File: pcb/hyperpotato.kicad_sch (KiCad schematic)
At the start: 61 parts, among them J1 Conn_01x02_Socket, J2 Conn_01x02_Socket, J3 Conn_01x04, J4 Conn_01x04, J5 Conn_01x04, J6 Conn_01x12_Socket, J7 Conn_01x12_Socket, K1 SW_Push, K10 SW_Push, K11 SW_Push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

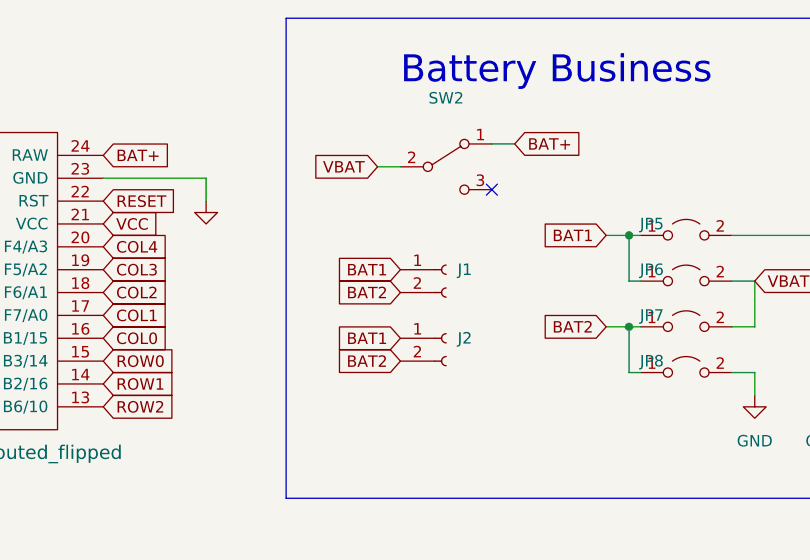
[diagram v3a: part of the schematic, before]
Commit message: Distribute components
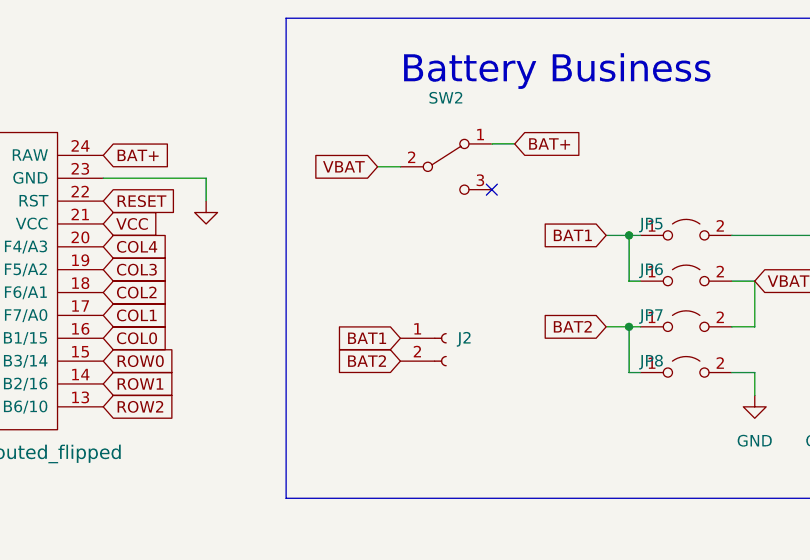
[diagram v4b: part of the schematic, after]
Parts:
- removed J1: Conn_01x02_Socket, hyperpotato:PinHeader_1x02_P2.54mm_Vertical, symbol Connector:Conn_01x02_Socket
- K17: footprint hyperpotato:V1_V2_HS_reversible_plated -> hyperpotato:V1_V2_HS_reversible_plated_no_fix_pin
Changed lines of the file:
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@@
-    )
-  )
-  (global_label "BAT1" (shape input) (at 219.71 45.72 180) (fields_autoplaced)
-    (effects (font (size 1.27 1.27)) (justify right))
-    (property "Intersheetrefs" "${INTERSHEET_REFS}" (at 212.1891 45.72 0)
-      (effects (font (size 1.27 1.27)) (justify right) hide)
     )
   )
@@
     (property "Intersheetrefs" "${INTERSHEET_REFS}" (at 256.422 114.3 0)
       (effects (font (size 1.27 1.27)) (justify left) hide)
-    )
-  )
-  (global_label "BAT2" (shape input) (at 219.71 48.26 180) (fields_autoplaced)
-    (effects (font (size 1.27 1.27)) (justify right))
-    (property "Intersheetrefs" "${INTERSHEET_REFS}" (at 212.1891 48.26 0)
-      (effects (font (size 1.27 1.27)) (justify right) hide)
     )
   )
@@
       (effects (font (size 1.27 1.27)) hide)
     )
-    (property "Footprint" "hyperpotato:V1_V2_HS_reversible_plated" (at 86.36 68.58 0)
+    (property "Footprint" "hyperpotato:V1_V2_HS_reversible_plated_no_fix_pin" (at 86.36 68.58 0)
       (effects (font (size 1.27 1.27)) hide)
     )
@@
         )
       )
-    )
-  )
-  (symbol (lib_id "Connector:Conn_01x02_Socket") (at 224.79 45.72 0) (unit 1)
-    (in_bom yes) (on_board yes) (dnp no)
-    (property "Reference" "J1" (at 226.06 45.72 0)
-      (effects (font (size 1.27 1.27)) (justify left))
-    )
-    (property "Value" "Conn_01x02_Socket" (at 226.06 48.26 0)
-      (effects (font (size 1.27 1.27)) (justify left) hide)
-    )
-    (property "Footprint" "hyperpotato:PinHeader_1x02_P2.54mm_Vertical" (at 224.79 45.72 0)
-      (effects (font (size 1.27 1.27)) hide)
-    )
-    (property "Datasheet" "~" (at 224.79 45.72 0)
-      (effects (font (size 1.27 1.27)) hide)
-    )
-    (pin "1")
-    (pin "2")
-    (instances
-      (project "hyperpotato"
-        (path "/65ee64f1-4704-447d-a409-ecee33d9a68d"
-          (reference "J1") (unit 1)
-        )
-      )
-      (project "koepckeae"
-        (path "/84582659-f20d-4b57-a904-d4b599b50d46"
-          (reference "J2") (unit 1)
-        )
-      )

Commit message: Finish v2
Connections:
- net COL0: now also U1.17 (F7/A0); no longer U1.16 (B1/15)
- net COL1: now also U1.16 (B1/15); no longer U1.17 (F7/A0)
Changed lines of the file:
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@@
     )
   )
-  (global_label "COL0" (shape input) (at 186.69 53.34 0) (fields_autoplaced)
+  (global_label "COL1" (shape input) (at 186.69 53.34 0) (fields_autoplaced)
     (effects (font (size 1.27 1.27)) (justify left))
     (property "Intersheetrefs" "${INTERSHEET_REFS}" (at 194.5133 53.34 0)
@@
     )
   )
-  (global_label "COL1" (shape input) (at 186.69 50.8 0) (fields_autoplaced)
+  (global_label "COL0" (shape input) (at 186.69 50.8 0) (fields_autoplaced)
     (effects (font (size 1.27 1.27)) (justify left))
     (property "Intersheetrefs" "${INTERSHEET_REFS}" (at 194.5133 50.8 0)

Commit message: Quick and dirty tucky thumbs pcb
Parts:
- removed C1: 2.2uF, hyperpotato:C_reversible, symbol Device:C
- removed J3: Conn_01x04, hyperpotato:Trackpoint_Connector_Reversible, symbol Connector_Generic:Conn_01x04
- removed J4, J5: Conn_01x04, hyperpotato:Trackpoint_Connector, symbol Connector_Generic:Conn_01x04
- removed J6, J7: Conn_01x12_Socket, hyperpotato:Trackpoint_PCB_Connector, symbol Connector:Conn_01x12_Socket
- removed R1, R2: 4.7k, hyperpotato:R_reversible, symbol Device:R
- removed R3: 100k, hyperpotato:R_reversible, symbol Device:R
- K1, K10, K11, K12, K13, K14, K16, K2, K3, K4, K5, K6, K7, K8, K9: footprint hyperpotato:V1_V2_HS_reversible_plated -> hyperpotato:PG1350_HS_reversible_plated
- K15: footprint hyperpotato:V1_V2_HS_reversible_plated_alt -> hyperpotato:PG1350_HS_reversible_plated
- K17: footprint hyperpotato:V1_V2_HS_reversible_plated_no_fix_pin -> hyperpotato:PG1350_HS_reversible_plated
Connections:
- net COL0: now also U1.15 (B3/14); no longer U1.17 (F7/A0)
- net COL2: now also U1.17 (F7/A0); no longer U1.18 (F6/A1)
- net COL3: now also U1.18 (F6/A1); no longer U1.19 (F5/A2)
- net COL4: now also K15.1, U1.19 (F5/A2); no longer K15.2, U1.20 (F4/A3)
- net ROW0: now also U1.20 (F4/A3); no longer U1.15 (B3/14)
- net ROW3: now also U1.11 (8/B4); no longer U1.9 (6/D7)
- net at D15.2 (A): now also K15.2; no longer K15.1
- net TP_CLK: no longer names the net of U1.2 (RX1/D2)
- net TP_DATA: no longer names the net of U1.1 (TX0/D3)
- no-connect marks 17 -> 5
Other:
- moved on the sheet: H1, H2, H3, H4

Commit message: Quick and dirty choc mini version
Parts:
- K1, K11, K6: footprint hyperpotato:PG1350_HS_reversible_plated -> hyperpotato:SW_PG1350_rev_DPB2.1; symbol hyperpotato:SW_Push -> Switch:SW_Push
- K10, K12, K13, K14, K15, K16, K17, K2, K3, K4, K5, K7, K8, K9: footprint hyperpotato:PG1350_HS_reversible_plated -> hyperpotato:Choc_Mini_PG1232_Choc_Spacing_dual_ease; symbol hyperpotato:SW_Push -> Switch:SW_Push
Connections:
- net ROW0: no longer K1.3, K2.3, K3.3, K4.3, K5.3
- net ROW1: no longer K10.3, K6.3, K7.3, K8.3, K9.3
- net ROW2: no longer K11.3, K12.3, K13.3, K14.3, K15.3
- net ROW3: no longer K16.3, K17.3
